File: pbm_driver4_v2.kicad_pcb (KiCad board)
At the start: 2 copper layers, 30 x 70 mm, 78 parts, among them J1 Conn_02x10_Odd_Even, J2 Conn_01x10, Q1 PSMN4R0-30YLDX, Q2 PSMN4R0-30YLDX, Q3 PSMN4R0-30YLDX, Q4 PSMN4R0-30YLDX, U1 ADA4099-2xR, U11 TS5A3159ADCK, U12 TS5A3159ADCK, U13 TS5A3159ADCK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

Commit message: Add PCB file to refactor.
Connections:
- net /Driver/REF1 renamed /Driver1/REF
- net /Driver/REF2 renamed /Driver2/REF
- net /Driver/REF3 renamed /Driver3/REF
- net /Driver/REF4 renamed /Driver4/REF
- net Net-(Q1-G) renamed /Driver1/GATE
- net Net-(Q2-G) renamed /Driver2/GATE
- net Net-(Q3-G) renamed /Driver3/GATE
- net Net-(Q4-G) renamed /Driver4/GATE
- net Net-(U21-+) renamed /Driver1/FILTER
- net Net-(U21--) renamed /Driver1/FILTER_FB
- net Net-(U22-+) renamed /Driver2/FILTER
- net Net-(U22--) renamed /Driver2/FILTER_FB
- net Net-(U23-+) renamed /Driver3/FILTER
- net Net-(U23--) renamed /Driver3/FILTER_FB
- net Net-(U24-+) renamed /Driver4/FILTER
- net Net-(U24--) renamed /Driver4/FILTER_FB
- C31 pad 1: Net-(C31-Pad1) -> /Driver1/FB
- C31 pad 2: Net-(U1A--) -> Net-(C31-Pad2)
- C32 pad 1: Net-(C32-Pad1) -> /Driver2/FB
- C32 pad 2: Net-(U1B--) -> Net-(C32-Pad2)
- C33 pad 1: Net-(C33-Pad1) -> /Driver3/FB
- C33 pad 2: Net-(U2A--) -> Net-(C33-Pad2)
- C34 pad 1: Net-(C34-Pad1) -> /Driver4/FB
- C34 pad 2: Net-(U2B--) -> Net-(C34-Pad2)
- Q1 pad 1: Net-(Q1-S-Pad1) -> /Driver1/SENSE_R
- Q1 pad 2: Net-(Q1-S-Pad1) -> /Driver1/SENSE_R
- Q1 pad 3: Net-(Q1-S-Pad1) -> /Driver1/SENSE_R
- Q2 pad 1: Net-(Q2-S-Pad1) -> /Driver2/SENSE_R
- Q2 pad 2: Net-(Q2-S-Pad1) -> /Driver2/SENSE_R
- Q2 pad 3: Net-(Q2-S-Pad1) -> /Driver2/SENSE_R
- Q3 pad 1: Net-(Q3-S-Pad1) -> /Driver3/SENSE_R
- Q3 pad 2: Net-(Q3-S-Pad1) -> /Driver3/SENSE_R
- Q3 pad 3: Net-(Q3-S-Pad1) -> /Driver3/SENSE_R
- Q4 pad 1: Net-(Q4-S-Pad1) -> /Driver4/SENSE_R
- Q4 pad 2: Net-(Q4-S-Pad1) -> /Driver4/SENSE_R
- Q4 pad 3: Net-(Q4-S-Pad1) -> /Driver4/SENSE_R
- R1 pad 1: Net-(Q1-S-Pad1) -> /Driver1/SENSE_R
- R11 pad 1: Net-(C31-Pad1) -> Net-(C31-Pad2)
- R12 pad 1: Net-(C32-Pad1) -> Net-(C32-Pad2)
- R13 pad 1: Net-(C33-Pad1) -> Net-(C33-Pad2)
- R14 pad 1: Net-(C34-Pad1) -> Net-(C34-Pad2)
- R2 pad 1: Net-(Q2-S-Pad1) -> /Driver2/SENSE_R
- R3 pad 1: Net-(Q3-S-Pad1) -> /Driver3/SENSE_R
- R31 pad 1: Net-(U1A--) -> /Driver1/SENSE_R
- R31 pad 2: Net-(Q1-S-Pad1) -> /Driver1/FB
- R32 pad 1: Net-(U1B--) -> /Driver2/SENSE_R
- R32 pad 2: Net-(Q2-S-Pad1) -> /Driver2/FB
- R33 pad 1: Net-(U2A--) -> /Driver3/SENSE_R
- R33 pad 2: Net-(Q3-S-Pad1) -> /Driver3/FB
- R34 pad 1: Net-(U2B--) -> /Driver4/SENSE_R
- R34 pad 2: Net-(Q4-S-Pad1) -> /Driver4/FB
- R4 pad 1: Net-(Q4-S-Pad1) -> /Driver4/SENSE_R
- R41 pad 2: Net-(Q1-S-Pad1) -> /Driver1/SENSE_R
- R42 pad 2: Net-(Q2-S-Pad1) -> /Driver2/SENSE_R
- R43 pad 2: Net-(Q3-S-Pad1) -> /Driver3/SENSE_R
- R44 pad 2: Net-(Q4-S-Pad1) -> /Driver4/SENSE_R
- U1 pad 1: Net-(C31-Pad1) -> Net-(C31-Pad2)
- U1 pad 2: Net-(U1A--) -> /Driver1/FB
- U1 pad 6: Net-(U1B--) -> /Driver2/FB
- U1 pad 7: Net-(C32-Pad1) -> Net-(C32-Pad2)
- U2 pad 1: Net-(C33-Pad1) -> Net-(C33-Pad2)
- U2 pad 2: Net-(U2A--) -> /Driver3/FB
- U2 pad 6: Net-(U2B--) -> /Driver4/FB
- U2 pad 7: Net-(C34-Pad1) -> Net-(C34-Pad2)

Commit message: Finished schematic refactor to six A-sheets. Updated PCB.
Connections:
- net /SPARE1 renamed /Connectors/SPARE1
- net /SPARE2 renamed /Connectors/SPARE2
- J1 pad 4: /DAC1 -> /DAC2

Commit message: Updated PCB stackup and design options
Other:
- copper layers 2 -> 4
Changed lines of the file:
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@@
 	(layers
 		(0 "F.Cu" signal)
+		(4 "In1.Cu" power)
+		(6 "In2.Cu" power)
 		(2 "B.Cu" signal)
 		(9 "F.Adhes" user "F.Adhesive")
@@
 		(pad_to_mask_clearance 0)
 		(allow_soldermask_bridges_in_footprints no)
-		(tenting front back)
+		(tenting none)
 		(pcbplotparams
 			(layerselection 0x00000000_00000000_55555555_5755f5ff)

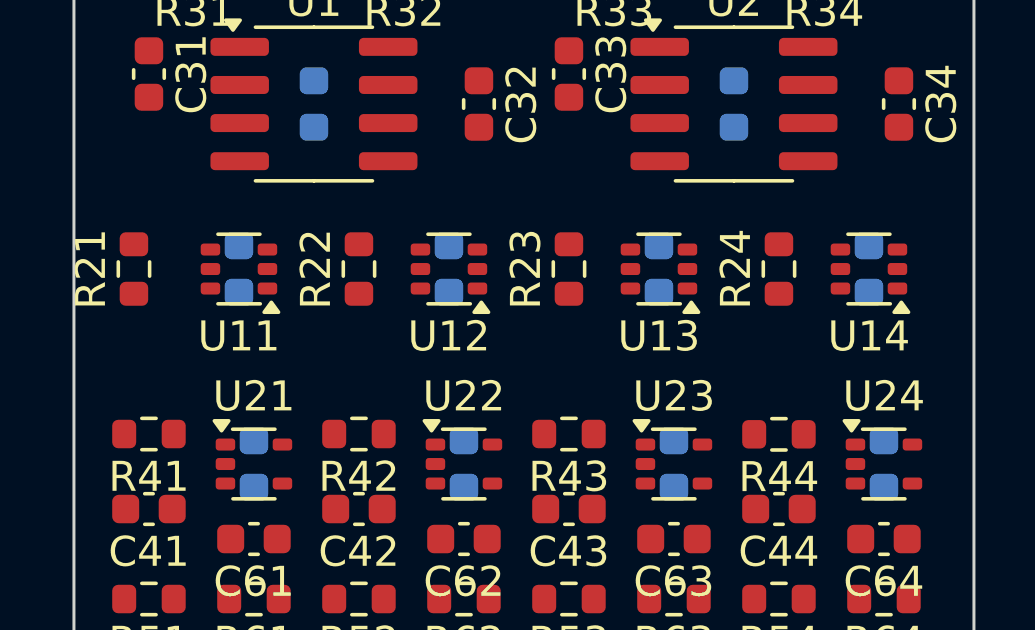
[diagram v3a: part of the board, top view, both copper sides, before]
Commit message: Added two 1x2 12V power connectors and 4x bypassing caps
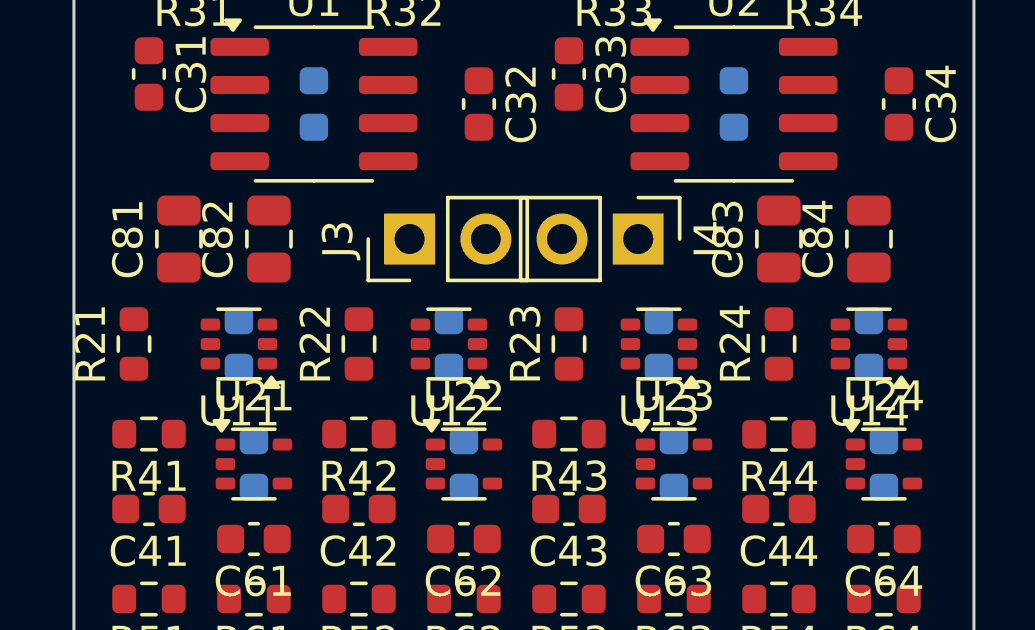
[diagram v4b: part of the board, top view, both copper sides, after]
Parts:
- added C81: 10UF 25V, $Local:C_0805_2012Metric, F.Cu at (3.50, -30.0)
- added C82: 10UF 25V, $Local:C_0805_2012Metric, F.Cu at (6.50, -30.0)
- added C83: 10UF 25V, $Local:C_0805_2012Metric, F.Cu at (23.5, -30.0)
- added C84: 10UF 25V, $Local:C_0805_2012Metric, F.Cu at (26.5, -30.0)
- added J3: Conn_01x02, $Local:PinHeader_1x02_P2.54mm_Vertical, F.Cu at (11.2, -30.0)
- added J4: Conn_01x02, $Local:PinHeader_1x02_P2.54mm_Vertical, F.Cu at (18.8, -30.0)
- moved C11 2.50 mm to (5.50, -26.5)
- moved C12 2.50 mm to (12.5, -26.5)
- moved C13 2.50 mm to (19.5, -26.5)
- moved C14 2.50 mm to (26.5, -26.5)
- moved R21 2.50 mm to (2.00, -26.5)
- moved R22 2.50 mm to (9.50, -26.5)
- moved R23 2.50 mm to (16.5, -26.5)
- moved R24 2.50 mm to (23.5, -26.5)
- moved U11 2.50 mm to (5.50, -26.5)
- moved U12 2.50 mm to (12.5, -26.5)
- moved U13 2.50 mm to (19.5, -26.5)
- moved U14 2.50 mm to (26.5, -26.5)

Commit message: Routing WIP
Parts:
- turned C31 to 90 degrees
- turned C32 to 90 degrees
- turned C33 to 90 degrees
- turned C34 to 90 degrees
- turned R31 to 0 degrees
- turned R32 to 0 degrees
- turned R33 to 0 degrees
- turned R34 to 0 degrees
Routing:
- net /Driver4/SENSE_R: track 0.00 -> 22.5 mm
- net GND: track 0.00 -> 20.4 mm, vias 0 -> 12
- net /Driver2/SENSE_R: track 0.00 -> 13.5 mm
- net /Driver1/SENSE_R: track 0.00 -> 13.5 mm
- net /Driver3/SENSE_R: track 0.00 -> 13.5 mm
- net /Driver4/FB: track 0.00 -> 12.2 mm
- net Net-(C31-Pad2): track 0.00 -> 11.1 mm
- net Net-(C33-Pad2): track 0.00 -> 11.1 mm
- net Net-(C32-Pad2): track 0.00 -> 10.9 mm
- net Net-(C34-Pad2): track 0.00 -> 10.9 mm
- net /LED1: track 0.00 -> 9.19 mm
- net /LED2: track 0.00 -> 8.39 mm
- net /LED4: track 0.00 -> 8.20 mm
- net /LED3: track 0.00 -> 7.60 mm
- net /Driver2/GATE: track 0.00 -> 4.92 mm
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- added copper zone on In2.Cu, net +12V
- added copper zone on In2.Cu, net +3.3V
- added copper zone on In1.Cu, net GND

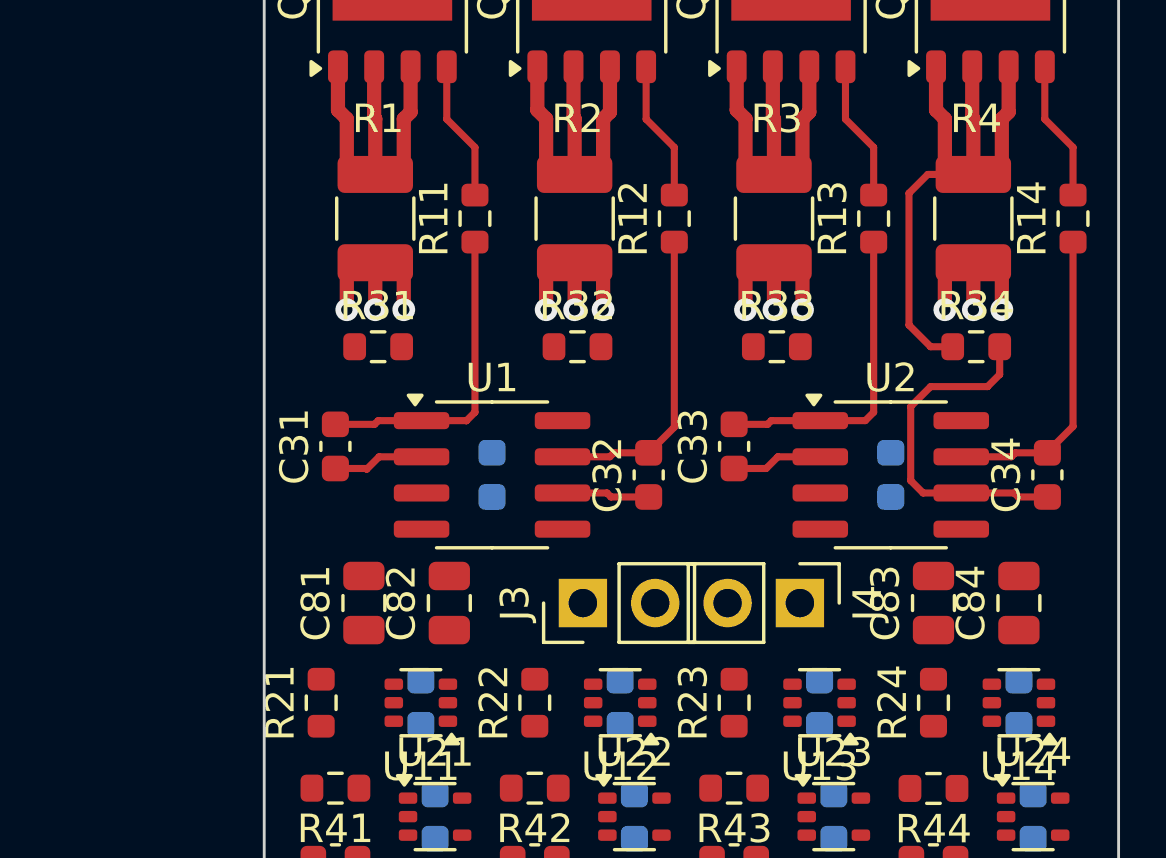
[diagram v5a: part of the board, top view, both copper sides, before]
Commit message: Routing WIP. Prep to look at SOT-23 op amps for U1 and U2. Added convenience link to Git Bash.
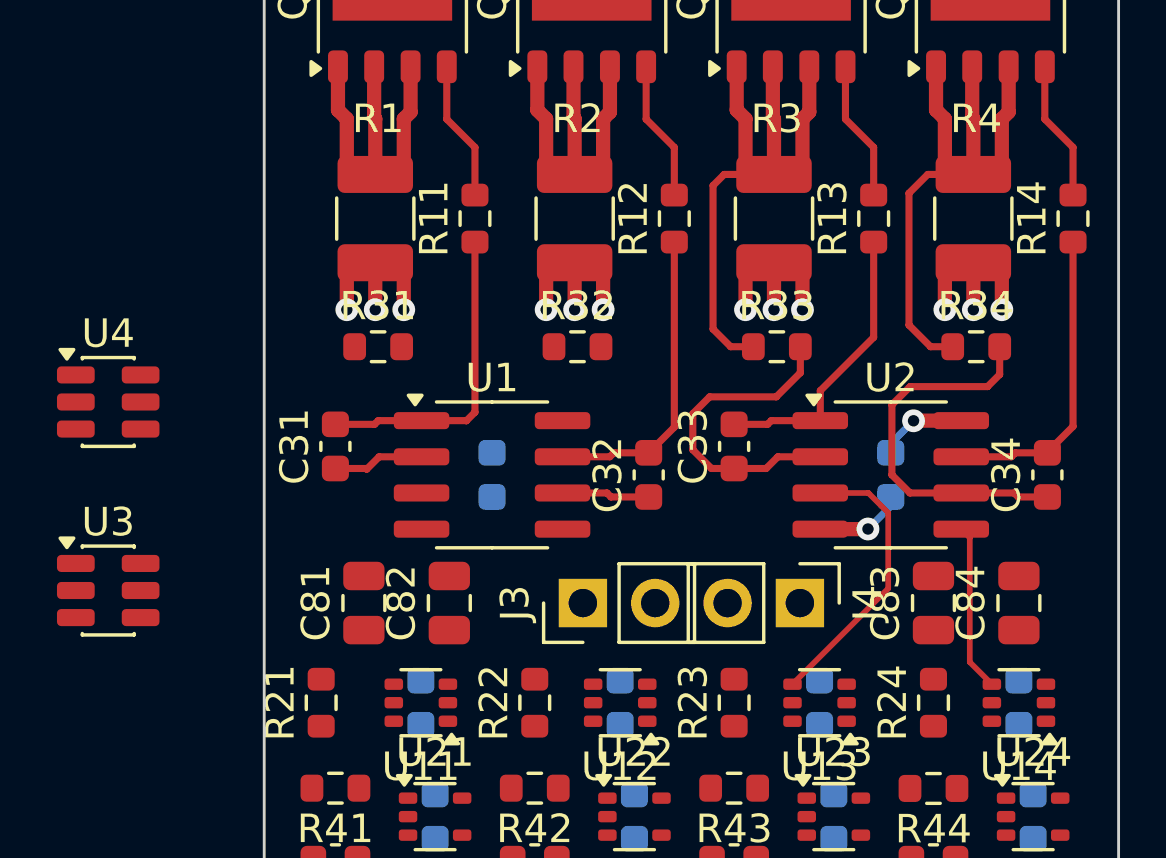
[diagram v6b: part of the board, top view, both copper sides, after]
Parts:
- added U3: ADA4099-2xR, Package_TO_SOT_SMD:TSOT-23-6, F.Cu at (-5.48, -30.4)
- added U4: ADA4099-2xR, Package_TO_SOT_SMD:TSOT-23-6, F.Cu at (-5.48, -37.1)
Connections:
- net Net-(C31-Pad2) renamed /Driver1/OUT
- net Net-(C32-Pad2) renamed /Driver2/OUT
- net Net-(C33-Pad2) renamed /Driver3/OUT
- net Net-(C34-Pad2) renamed /Driver4/OUT
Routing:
- net /Driver3/REF: track 0.00 -> 10.1 mm
- net /Driver3/SENSE_R: track 13.5 -> 22.5 mm
- net /Driver3/FB: track 3.19 -> 11.5 mm
- net /Driver4/REF: track 0.00 -> 5.89 mm
- net GND: track 20.4 -> 23.5 mm, vias 12 -> 13
- net +12V: track 0.00 -> 3.13 mm, vias 0 -> 1
- net /Driver4/FB: track 12.2 -> 13.4 mm
- net /Driver3/OUT: track 11.1 -> 10.1 mm

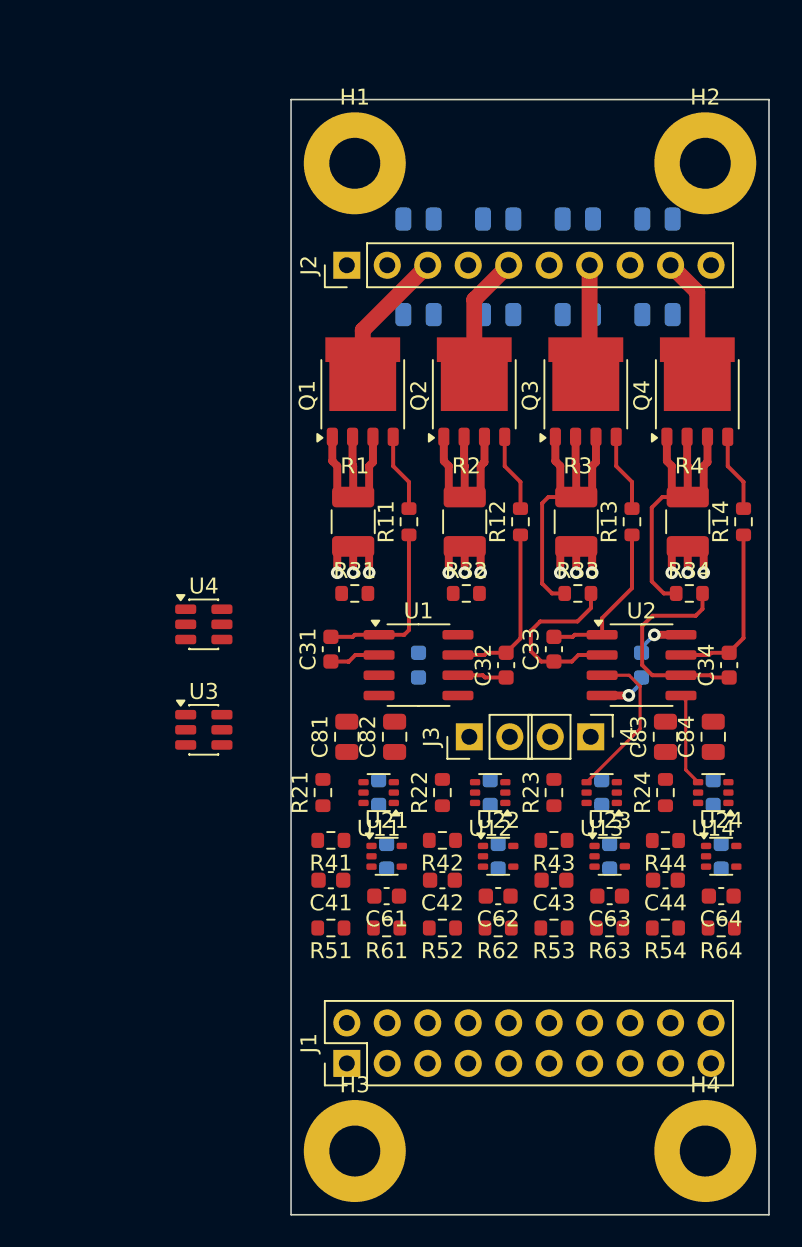
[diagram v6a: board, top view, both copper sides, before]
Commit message: Routing WIP with SOT-23 op amps
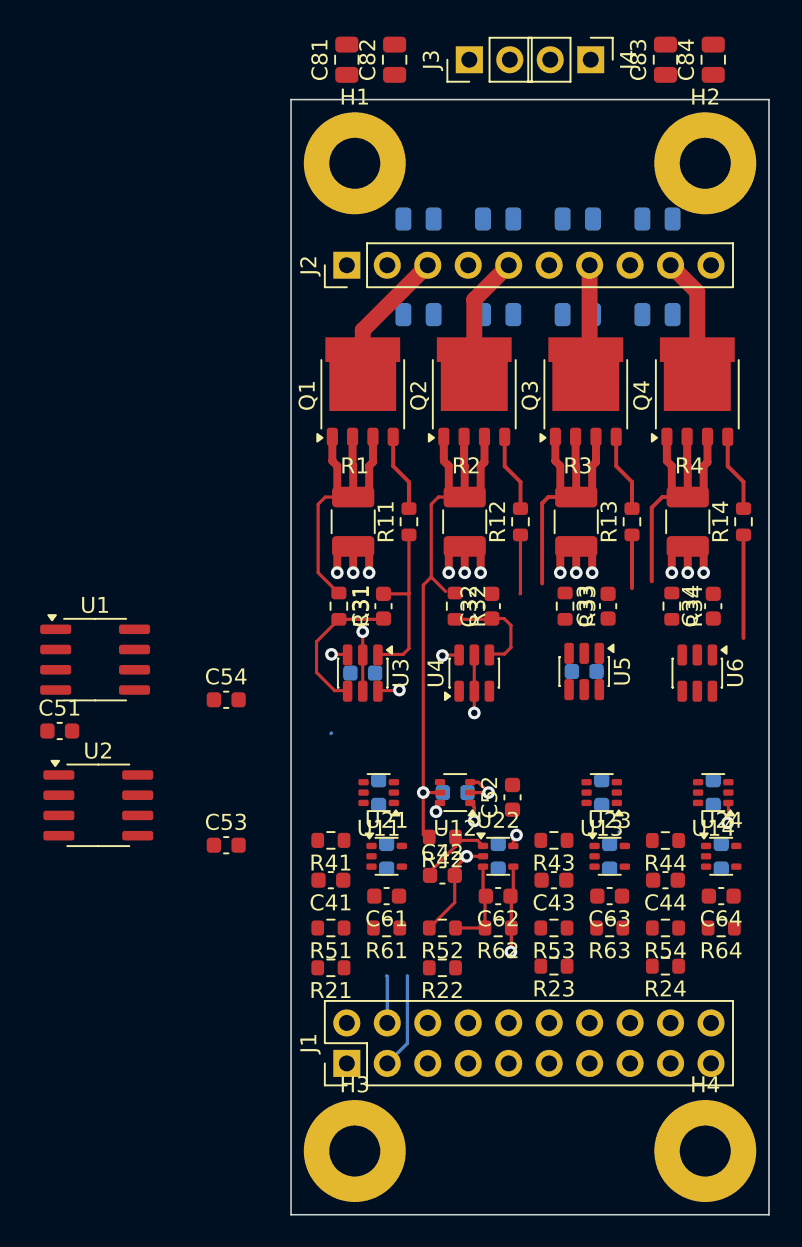
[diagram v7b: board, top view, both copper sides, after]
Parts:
- added C51: 100pF, $Local:C_0603_1608Metric, F.Cu at (-14.5, -30.4)
- added C52: 100pF, $Local:C_0603_1608Metric, F.Cu at (13.9, -26.2)
- added C53: 100pF, $Local:C_0603_1608Metric, F.Cu at (-4.07, -23.2)
- added C54: 100pF, $Local:C_0603_1608Metric, F.Cu at (-4.07, -32.3)
- added U5: ADA4099-2xR, Package_TO_SOT_SMD:TSOT-23-6, F.Cu at (18.4, -34.1)
- added U6: ADA4099-2xR, Package_TO_SOT_SMD:TSOT-23-6, F.Cu at (25.5, -34.0)
- moved C81 42.5 mm to (3.50, -72.5)
- moved C82 42.5 mm to (6.50, -72.5)
- moved C83 42.5 mm to (23.5, -72.5)
- moved C84 42.5 mm to (26.5, -72.5)
- moved J3 42.5 mm to (11.2, -72.5)
- moved J4 42.5 mm to (18.8, -72.5)
- moved U2 35.2 mm to (-12.1, -25.7)
- moved U1 20.3 mm to (-12.3, -34.8)
- moved U4 17.3 mm to (11.5, -34.0), turned to 90 degrees
- moved R21 11.0 mm to (2.50, -15.5), turned to 180 degrees
- moved R22 11.0 mm to (9.50, -15.5), turned to 180 degrees
- moved R23 10.9 mm to (16.5, -15.6), turned to 180 degrees
- moved R24 10.9 mm to (23.5, -15.6), turned to 180 degrees
- moved U3 10.6 mm to (4.50, -34.0), turned to -90 degrees
- moved C33 4.34 mm to (19.9, -38.2)
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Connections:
- U3 pad 5: unconnected-(U3-~{SHDN}-Pad5) -> GND
- U4 pad 5: unconnected-(U4-~{SHDN}-Pad5) -> GND
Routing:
- net /Driver2/SENSE_R: track 13.5 -> 38.5 mm
- net /Driver4/FB: track 13.4 -> 0.00 mm
- net GND: track 23.5 -> 36.8 mm, vias 13 -> 16
- net /Driver3/FB: track 11.5 -> 0.00 mm
- net /Driver3/REF: track 10.1 -> 0.00 mm
- net /Driver1/SENSE_R: track 13.5 -> 22.0 mm
- net /Driver2/OUT: track 10.9 -> 3.71 mm
- net /Driver3/OUT: track 10.1 -> 3.34 mm
- net /DAC1: track 0.00 -> 6.06 mm
- net /Driver1/FB: track 3.22 -> 9.16 mm
- net /Driver4/REF: track 5.89 -> 0.00 mm
- net /Driver2/FILTER_FB: track 0.00 -> 5.79 mm
- net /DAC2: track 0.00 -> 5.47 mm, vias 0 -> 2
- net /SENSE2: track 0.00 -> 5.45 mm, vias 0 -> 1
- net /Driver2/FILTER: track 0.00 -> 5.03 mm
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
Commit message: Exploring op amp rounting options.
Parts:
- removed U1, U2: ADA4099-2xR, $Local:SOIC-8_3.9x4.9mm_P1.27mm
- moved C2 7.99 mm to (26.3, -32.9)
- moved R33 6.22 mm to (17.7, -32.0), turned to 90 degrees
- moved C33 6.21 mm to (19.5, -32.0), turned to -90 degrees
- moved U5 2.40 mm to (18.4, -36.5)
- turned U6 to 180 degrees
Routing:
- net /Driver4/REF: track 0.00 -> 13.4 mm, vias 0 -> 1
- net /Driver3/SENSE_R: track 20.9 -> 33.2 mm
- net /Driver3/REF: track 0.00 -> 12.2 mm, vias 0 -> 1
- net /Driver2/OUT: track 3.71 -> 15.9 mm, vias 0 -> 2
- net /Driver3/OUT: track 3.34 -> 14.7 mm
- net GND: track 36.8 -> 45.7 mm, vias 16 -> 18
- net /Driver1/SENSE_R: track 22.0 -> 30.3 mm
- net /Driver1/REF: track 1.07 -> 8.47 mm
- net /Driver4/OUT: track 6.47 -> 13.5 mm
- net /Driver4/FB: track 0.00 -> 5.24 mm
- net /Driver2/REF: track 0.00 -> 4.48 mm
- net /Driver3/FB: track 0.00 -> 4.46 mm
- net +12V: track 2.43 -> 6.51 mm, vias 2 -> 4
- net /Driver4/SENSE_R: track 20.7 -> 22.3 mm
- net /Driver2/SENSE_R: track 38.5 -> 39.3 mm
